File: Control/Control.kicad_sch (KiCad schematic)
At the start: 80 parts, among them J1 Conn_02x08_Odd_Even, J2 Conn_02x08_Odd_Even, U1 74AHC1G04, U2 74HC73, U3 74LS161, U4 SST39SF020, U5 SST39SF020, U6 SST39SF020, U7 SST39SF020

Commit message: Control Unit first draft
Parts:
- added J4: MCR-MCRI, Connector_PinHeader_2.54mm:PinHeader_1x02_P2.54mm_Vertical, symbol Connector:Conn_01x02_Pin
- added J? (x2): Conn_01x02, symbol Connector_Generic:Conn_01x02
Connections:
- net PCE: now also J?.1 (Pin_1); no longer U7.17 (D3)
- net ~{PCL}: now also J?.1 (Pin_1); no longer U7.20 (D6)
- net at U3.1 (~{MR}): now also J4.1 (Pin_1)
- new net MCR: J4.2 (Pin_2)
- new net PCEi: U7.17 (D3)
- new net jump logic/PCE: J?.2 (Pin_2)
- new net jump logic/~{PCL}: J?.2 (Pin_2)
- new net ~{PCL}i: U7.20 (D6)
- no-connect marks 9 -> 10
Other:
- added sheet ALU interface (aluinterface.kicad_sch)
- added sheet jump logic (jump logic.kicad_sch)
- added sheet register interface (reg_interface.kicad_sch)
- moved on the sheet: C1, C2, U1, U3

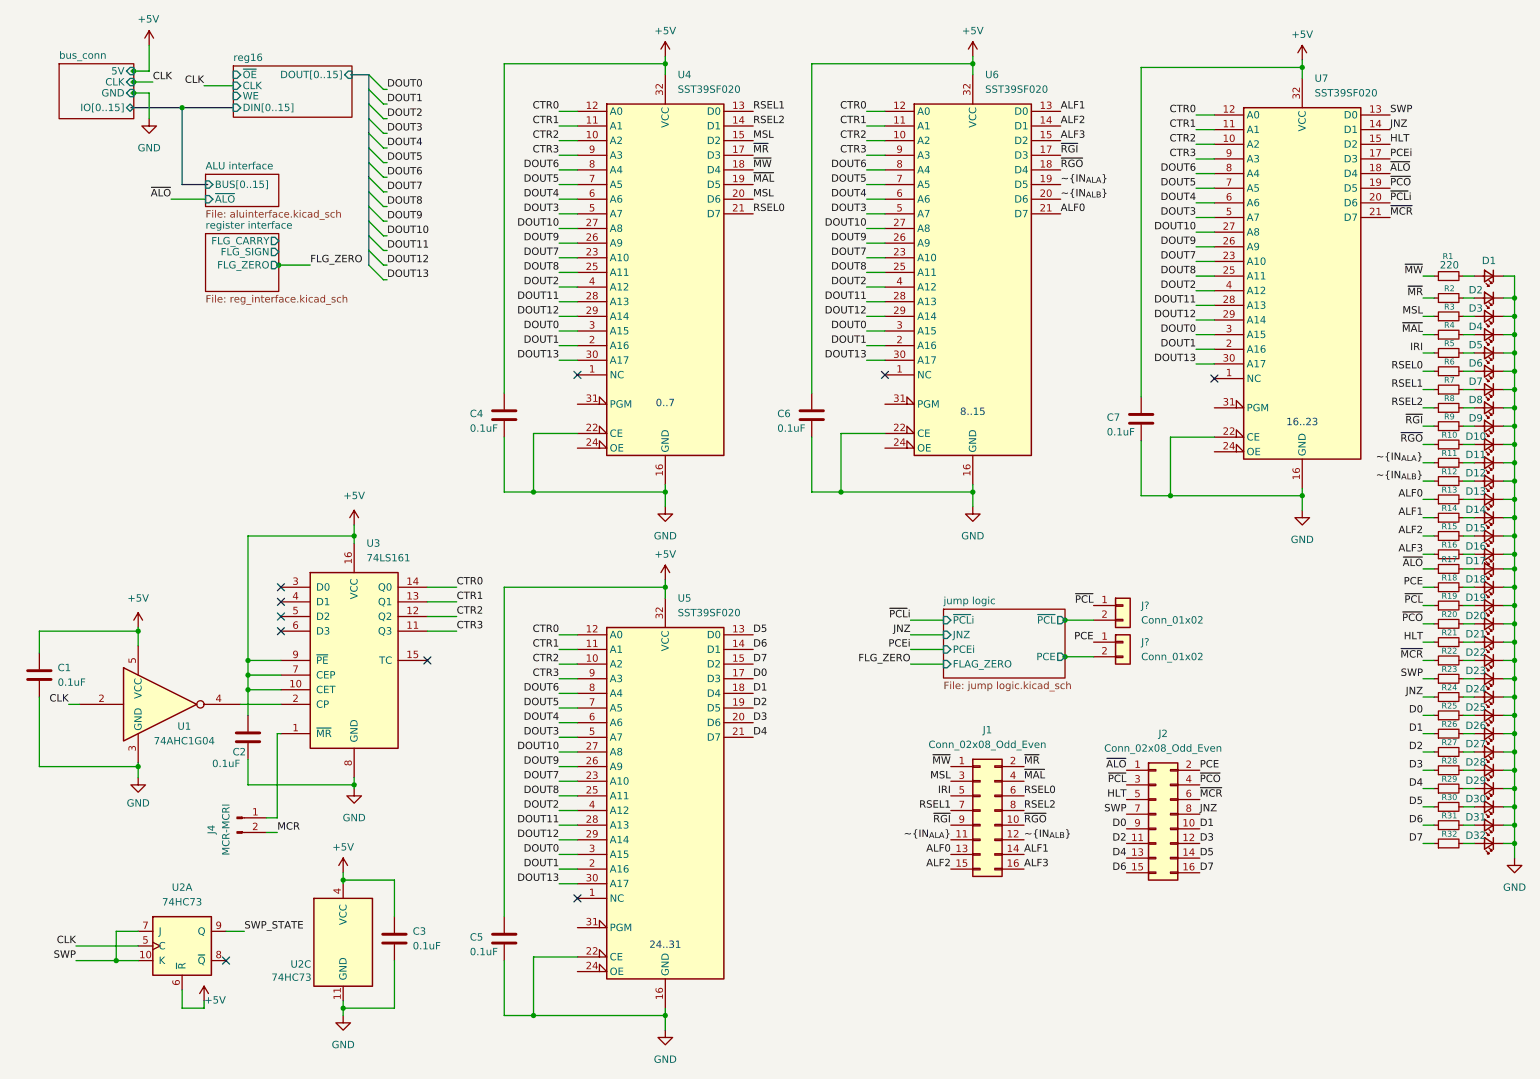
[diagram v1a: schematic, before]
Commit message: Cleanup, added photos and README overhaul
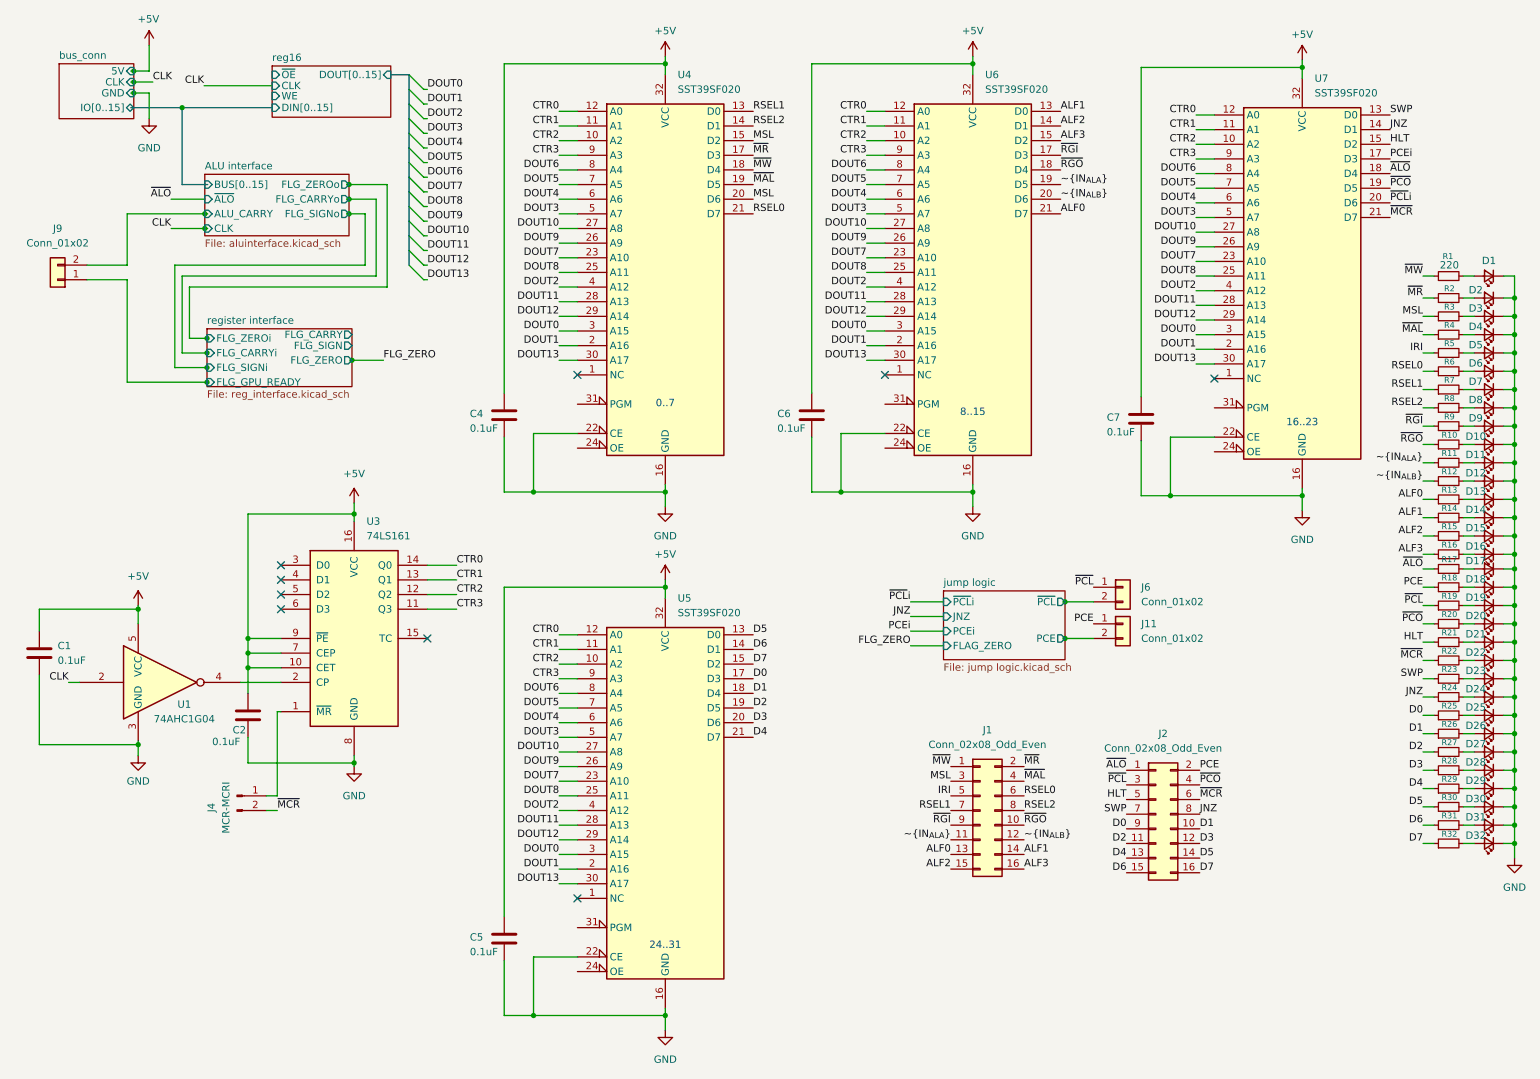
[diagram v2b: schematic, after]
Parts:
- removed C3: 0.1uF, Capacitor_SMD:C_0603_1608Metric, symbol Device:C
- removed U2: 74HC73, Package_SO:SOIC-14_3.9x8.7mm_P1.27mm, symbol 74xx:74LS73
- added J9: Conn_01x02, Connector_PinHeader_2.54mm:PinHeader_1x02_P2.54mm_Vertical, symbol Connector_Generic:Conn_01x02
- J11, J6: renamed from J?; footprint (none) -> Connector_PinHeader_2.54mm:PinHeader_1x02_P2.54mm_Vertical
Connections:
- net MCR is gone; now on net ~{MCR}: J4.2 (Pin_2)
- new net ALU interface/ALU_CARRY: J9.2 (Pin_2)
- new net register interface/FLG_GPU_READY: J9.1 (Pin_1)
- no-connect marks 10 -> 9
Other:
- sheet ALU interface ports: added ALU_CARRY, CLK, FLG_CARRYo, FLG_SIGNo, FLG_ZEROo; removed none
- sheet register interface ports: added FLG_CARRYi, FLG_GPU_READY, FLG_SIGNi, FLG_ZEROi; removed none
- moved on the sheet: C1, C2, J11, J4, J6, U1, U3

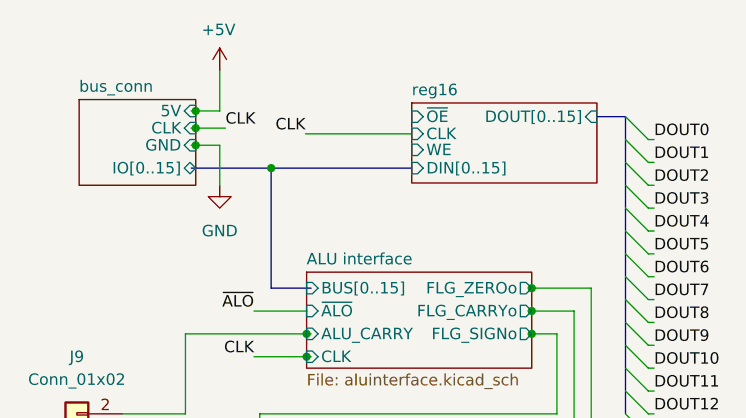
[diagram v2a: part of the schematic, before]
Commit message: Finalized Control unit for fabrication
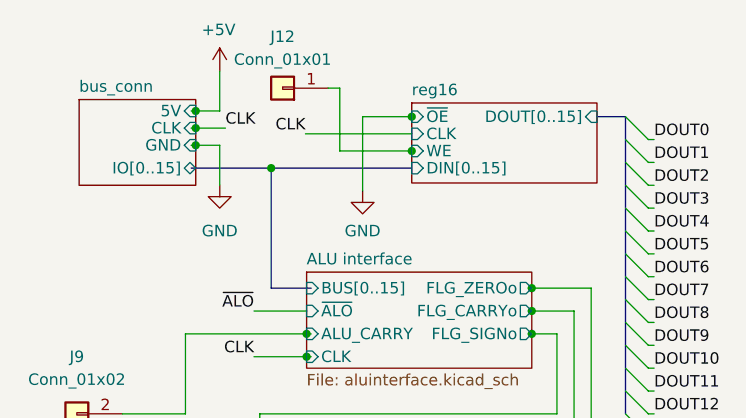
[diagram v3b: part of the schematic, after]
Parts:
- added J12: Conn_01x01, Connector_PinHeader_2.54mm:PinHeader_1x01_P2.54mm_Vertical, symbol Connector_Generic:Conn_01x01
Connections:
- net reg16/WE: now also J12.1 (Pin_1)
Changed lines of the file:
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@@
 	)
 	(junction
+		(at 57.531 26.67)
+		(diameter 0)
+		(color 0 0 0 0)
+	)
+	(junction
 		(at 70.866 46.99)
 		(diameter 0)
@@
 	)
 	(junction
+		(at 57.531 22.86)
+		(diameter 0)
+		(color 0 0 0 0)
+	)
+	(junction
 		(at 273.05 133.985)
 		(diameter 0)
@@
 	(wire
 		(pts
+			(xy 57.531 26.67) (xy 57.785 26.67)
+		)
+		(stroke
+			(width 0)
+			(type default)
+		)
+	)
+	(wire
+		(pts
 			(xy 160.655 29.21) (xy 163.83 29.21)
 		)
@@
 	(wire
 		(pts
+			(xy 57.785 22.86) (xy 57.531 22.86)
+		)
+		(stroke
+			(width 0)
+			(type default)
+		)
+	)
+	(wire
+		(pts
 			(xy 97.79 20.955) (xy 125.73 20.955)
 		)
@@
 	(wire
 		(pts
+			(xy 57.531 22.86) (xy 52.07 22.86)
+		)
+		(stroke
+			(width 0)
+			(type default)
+		)
+	)
+	(wire
+		(pts
 			(xy 264.16 143.51) (xy 266.065 143.51)
 		)
@@
 	(wire
 		(pts
+			(xy 48.26 19.685) (xy 49.53 19.685)
+		)
+		(stroke
+			(width 0)
+			(type default)
+		)
+	)
+	(wire
+		(pts
 			(xy 33.02 24.13) (xy 33.528 24.13)
 		)
@@
 	(wire
 		(pts
+			(xy 49.53 19.685) (xy 49.53 26.67)
+		)
+		(stroke
+			(width 0)
+			(type default)
+		)
+	)
+	(wire
+		(pts
 			(xy 273.05 114.935) (xy 273.05 118.11)
 		)
@@
 	(wire
 		(pts
+			(xy 49.53 26.67) (xy 57.531 26.67)
+		)
+		(stroke
+			(width 0)
+			(type default)
+		)
+	)
+	(wire
+		(pts
 			(xy 32.385 55.88) (xy 32.385 46.99)
 		)
@@
 	(wire
 		(pts
+			(xy 52.07 22.86) (xy 52.07 31.115)
+		)
+		(stroke
+			(width 0)
+			(type default)
+		)
+	)
+	(wire
+		(pts
 			(xy 257.175 102.87) (xy 259.08 102.87)
 		)
@@
 	)
 	(symbol
+		(lib_id "power:GND")
+		(at 52.07 31.115 0)
+		(unit 1)
+		(exclude_from_sim no)
+		(in_bom yes)
+		(on_board yes)
+		(dnp no)
+		(fields_autoplaced yes)
+		(property "Reference" "#PWR05"
+			(at 52.07 37.465 0)
+			(effects
+				(font
+					(size 1.27 1.27)
+				)
+				(hide yes)
+			)
+		)
+		(property "Value" "GND"
+			(at 52.07 35.56 0)
+			(effects
+				(font
+					(size 1.27 1.27)
+				)
+			)
+		)
+		(property "Footprint" ""
+			(at 52.07 31.115 0)
+			(effects
+				(font
+					(size 1.27 1.27)
+				)
+				(hide yes)
+			)
+		)
+		(property "Datasheet" ""
+			(at 52.07 31.115 0)
+			(effects
+				(font
+					(size 1.27 1.27)
+				)
+				(hide yes)
+			)
+		)
+		(property "Description" "Power symbol creates a global label with name \"GND\" , ground"
+			(at 52.07 31.115 0)
+			(effects
+				(font
+					(size 1.27 1.27)
+				)
+				(hide yes)
+			)
+		)
+		(pin "1"
+		)
+		(instances
+			(project ""
+				(path "/0a4a6030-43dc-471b-9d34-a62eb343ab9f"
+					(reference "#PWR05")
+					(unit 1)
+				)
+			)
+		)
+	)
+	(symbol
 		(lib_id "Device:R_Small")
 		(at 261.62 108.585 90)
@@
 	)
 	(symbol
+		(lib_id "Connector_Generic:Conn_01x01")
+		(at 43.18 19.685 180)
+		(unit 1)
+		(exclude_from_sim no)
+		(in_bom yes)
+		(on_board yes)
+		(dnp no)
+		(fields_autoplaced yes)
+		(property "Reference" "J12"
+			(at 43.18 13.97 0)
+			(effects
+				(font
+					(size 1.27 1.27)
+				)
+			)
+		)
+		(property "Value" "Conn_01x01"
+			(at 43.18 16.51 0)
+			(effects
+				(font
+					(size 1.27 1.27)
+				)
+			)
+		)
+		(property "Footprint" "Connector_PinHeader_2.54mm:PinHeader_1x01_P2.54mm_Vertical"
+			(at 43.18 19.685 0)
+			(effects
+				(font
+					(size 1.27 1.27)
+				)
+				(hide yes)
+			)
+		)
+		(property "Datasheet" "~"
+			(at 43.18 19.685 0)
+			(effects
+				(font
+					(size 1.27 1.27)
+				)
+				(hide yes)
+			)
+		)
+		(property "Description" "Generic connector, single row, 01x01, script generated (kicad-library-utils/schlib/autogen/connector/)"
+			(at 43.18 19.685 0)
+			(effects
+				(font
+					(size 1.27 1.27)
+				)
+				(hide yes)
+			)
+		)
+		(pin "1"
+		)
+		(instances
+			(project ""
+				(path "/0a4a6030-43dc-471b-9d34-a62eb343ab9f"
+					(reference "J12")
+					(unit 1)
+				)
+			)
+		)
+	)
+	(symbol
 		(lib_id "Device:LED_Small")
 		(at 268.605 93.345 180)
@@
 		)
 		(pin "WE" input
-			(at 57.531 26.543 180)
+			(at 57.531 26.67 180)
 			(effects
 				(font

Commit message: Updated control unit and finalized for fabrication
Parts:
- added TP5, TP6, TP7, TP8: TestPoint, TestPoint:TestPoint_Pad_D1.0mm, symbol Connector:TestPoint
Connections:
- net +5V: now also U4.31 (PGM), U5.31 (PGM), U6.31 (PGM), U7.31 (PGM)
- net CTR0: now also TP5.1
- net CTR1: now also TP7.1
- net CTR2: now also TP8.1
- net CTR3: now also TP6.1
- net GND: now also U4.24 (OE), U5.24 (OE), U6.24 (OE), U7.24 (OE)
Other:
- sheet register interface ports: added CLK; removed FLG_CARRY, FLG_SIGN
